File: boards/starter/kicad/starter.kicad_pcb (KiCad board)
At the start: 2 copper layers, 50 x 50 mm, 37 parts, among them J1 USB-C, J2 Qwiic, SW1 RESET, SW2 BOOT, U1 ESP32-S3-WROOM-1-N16R8, U2 LDL1117S33R, U3 H5VUT2U, U4 SHT40-AD1B

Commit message: Phase 1 complete: SWIG crash fixed, all gates pass, fab files, reviews
- Segfault root cause: pcbnew's Remove() and Outline()/GetCourtyard() hand
  KiCad-owned memory to Python; fixed (leak removed items, borrowed()).
  Each stage and each SWIG step now runs in its own process; zones are
  filled by kicad-cli (D-011)
- Routing: pours hidden from Freerouting so GND gets real tracks; Power
  class 0.3 mm; retries; stitching checks track clearance (D-012)
- New gates: netlist round trip, net-class patterns, routing report
- fab.py: gerbers/drill zip, JLCPCB BOM and CPL with rotation corrections
- Datasheet check and blind review by separate agents; cap values, fuse
  before TVS, C1 placement, USB net class fixed (D-014)
- Stack survey confirms the stack (D-013)

Co-Authored-By: Claude Opus 5.5 <noreply@anthropic.com>
Claude-Session: https://claude.ai/code/session_01EfFHJzgmcgpgRkWALfogi6
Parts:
- C2: value 22u -> 1u
- C3: value 10u -> 22u
- moved C1 3.89 mm to (107.5, 131.8), turned to 180 degrees
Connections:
- D3 pad 1: VBUS -> +5V
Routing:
- net GND: track 0.75 -> 233.4 mm, vias 58 -> 74
- net /I2C_SCL: track 57.2 -> 31.1 mm, vias 2 -> 0
- net +5V: track 24.4 -> 36.2 mm
- net VBUS: track 34.1 -> 27.0 mm, vias 0 -> 2
- net /I2C_SDA: track 35.0 -> 41.5 mm, vias 0 -> 4
- net /USB_D+: track 35.4 -> 29.5 mm, vias 2 -> 3
- net /EN: track 42.8 -> 47.2 mm, vias 2 -> 3
- net +3V3: track 111.0 -> 114.0 mm
- net /USB_D-: track 32.3 -> 31.0 mm
- net /BOOT: track 29.5 -> 28.4 mm
- net /UART_TX: track 11.8 -> 12.9 mm, vias 0 -> 2
- net /UART_RX: vias 2 -> 0

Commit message: Starter: LDO cooling copper, 0.3 mm ESP32 EPAD holes, 0.75 A fuse (D-015)
- pcbgen: CopperZone (local pour of one net, above GND) and
  RouteOptions.stitch_local (per-net via stitching); routing report now
  lists every pour and vias per net.
- Starter: +3V3 pour on both layers under U2's tab with 20 vias.
- Local footprint lib/footprints/pcbgen.pretty/ESP32-S3-WROOM-1_EPAD-Drill0.3:
  KiCad's footprint with the 12 EPAD drills at 0.3 mm (JLCPCB's quote form
  charges ~$50 for 0.2 mm).
- F1: Bourns MF-NSMF075-2 (C89653), which has a published derating table;
  a 0.5 A PTC holds only ~0.35-0.40 A at 50-60 C.
- Research: research/2026-09-29-holes-and-fuse.md.
- Full run: ERC 0, DRC 0 open (11 waived silk), 0 unrouted.

Co-Authored-By: Claude Opus 5.5 <noreply@anthropic.com>
Claude-Session: https://claude.ai/code/session_01QxXhFJGsvChPbjPevYQU4a
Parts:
- F1: value 500mA -> 750mA
- U1: footprint RF_Module:ESP32-S3-WROOM-1 -> pcbgen:ESP32-S3-WROOM-1_EPAD-Drill0.3
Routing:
- net /I2C_SDA: track 41.5 -> 59.2 mm, vias 4 -> 2
- net +3V3: track 114.0 -> 105.0 mm, vias 2 -> 22
- net VBUS: track 27.0 -> 18.4 mm, vias 2 -> 3
- net /USB_D+: track 29.5 -> 25.9 mm
- net /EN: track 47.2 -> 43.6 mm, vias 3 -> 2
- net /BOOT: track 28.4 -> 31.6 mm
- net +5V: track 36.2 -> 34.0 mm
- net GND: track 233.4 -> 231.7 mm, vias 74 -> 54
- net /USB_D-: track 31.0 -> 32.1 mm
- net /UART_RX: track 14.1 -> 14.8 mm, vias 0 -> 2
- added copper zone on B.Cu, net +3V3
- added copper zone on F.Cu, net +3V3

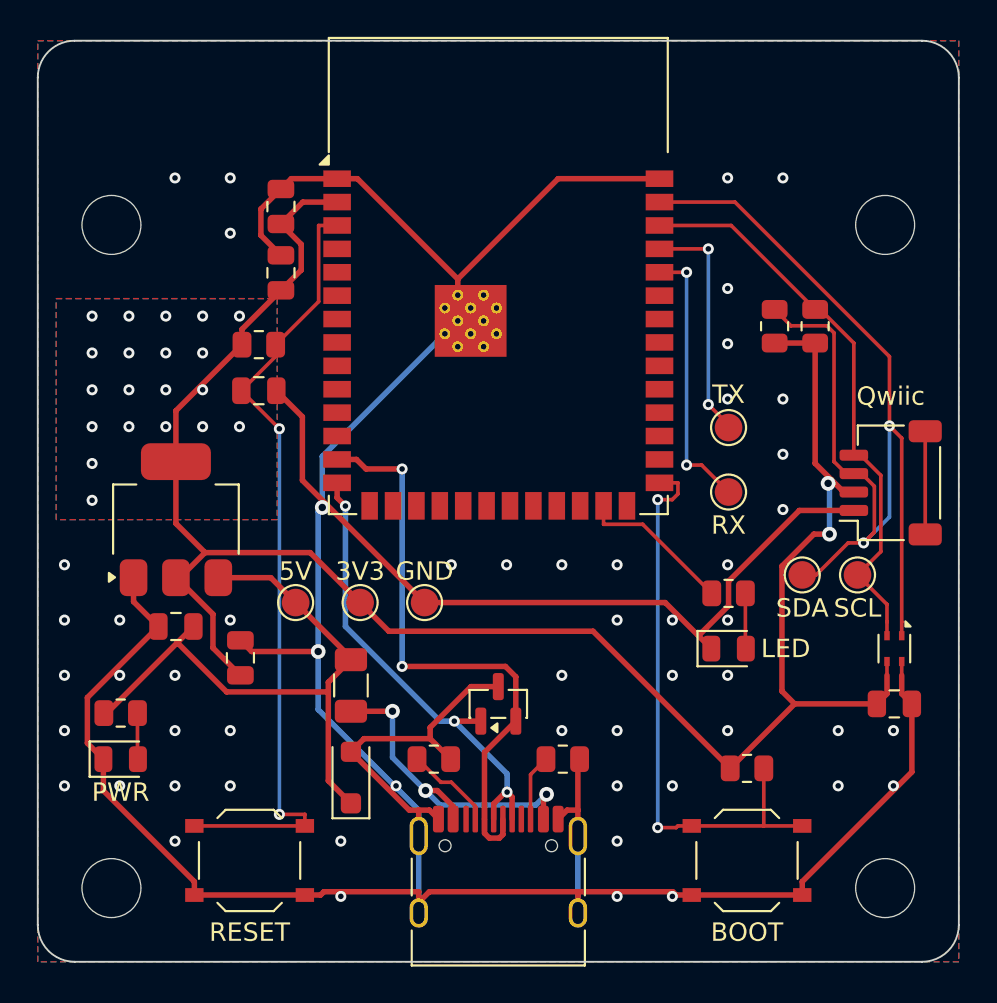
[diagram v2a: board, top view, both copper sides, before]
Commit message: Rust pcbgen: DSN writer, SES reader, stitching, report and fab
The route stage now writes the Specctra DSN itself and reads the SES
back (no SWIG); stitching reads the zone fill kicad-cli saved.

Checked on the starter board:
- DSN equal to KiCad's export in boundary, vias, rules, keep-outs,
  every pin's position/rotation/shape, nets, classes and locked stubs.
- Freerouting turned out deterministic (the same DSN routes the same
  twice); the Python run-to-run variation came from pcbnew's random
  footprint UUIDs reordering the DSN. Retries now shuffle the
  footprint order with a seed, so each try differs but stays
  reproducible.
- Full Rust run in place: netlist + net classes PASS, ERC 0, DRC 0
  open (same 11 waived silk warnings, 0 unconnected, parity 0),
  routing 0 unrouted, no copper in keep-outs, 20 +3V3 cooling vias,
  smallest drill 0.3 mm. BOM and CPL byte-identical to the Python
  ones; tracks differ (a new router run).

Co-Authored-By: Claude Opus 5.5 <noreply@anthropic.com>
Claude-Session: https://claude.ai/code/session_01Gx8G6vBFXfvHWNjYGCm7nX
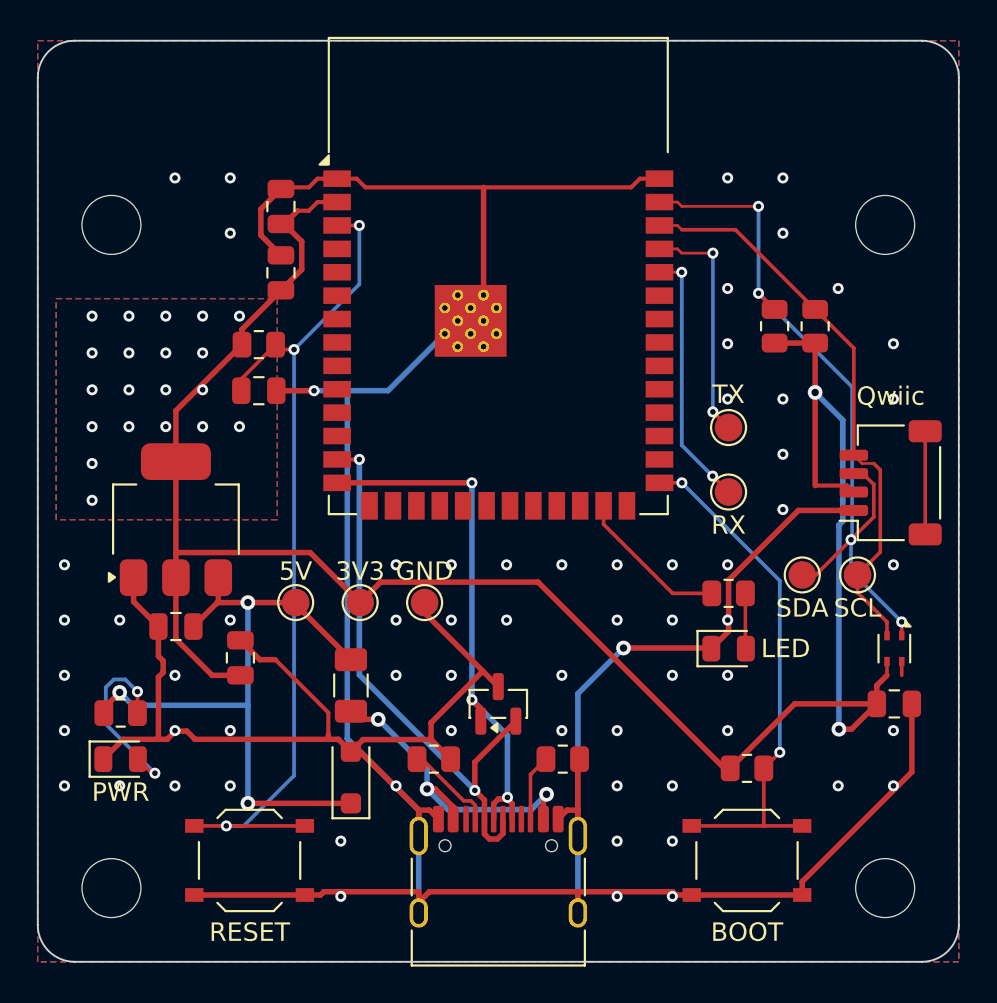
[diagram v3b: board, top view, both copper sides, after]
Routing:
- net /I2C_SDA: track 59.2 -> 41.6 mm, vias 2 -> 4
- net +3V3: track 105.0 -> 115.2 mm
- net /PWR_LED: track 2.51 -> 10.3 mm, vias 0 -> 2
- net /EN: track 43.6 -> 47.7 mm, vias 2 -> 3
- net /USB_D+: track 25.9 -> 29.5 mm
- net /BOOT: track 31.6 -> 28.4 mm
- net +5V: track 34.0 -> 37.0 mm, vias 0 -> 3
- net GND: track 231.7 -> 229.5 mm, vias 54 -> 65
- net /USB_D-: track 32.1 -> 31.1 mm
- net VBUS: track 18.4 -> 17.7 mm
- net /UART_RX: track 14.8 -> 14.2 mm

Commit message: starter: re-route with best-of-8 orders and fanout off (D-017)
Kept order 2 of 8: 0 unrouted, 20 routed vias (was 30), no routed track
under its class width (only the locked 0.2 mm escape stubs, 1.6 mm; was
45.9 mm). All gates pass: netlist and net classes PASS, ERC 0, DRC 0 open
(the same 11 waived silk warnings, 0 unconnected, parity 0), routing 0
unrouted, no copper in keep-outs. Parts, nets, placement and rules are
unchanged; schematic, BOM, CPL and positions byte-identical. Only the
copper layers and drill file changed (the other gerbers only in their
timestamps).

Co-Authored-By: Claude Opus 5.5 <noreply@anthropic.com>
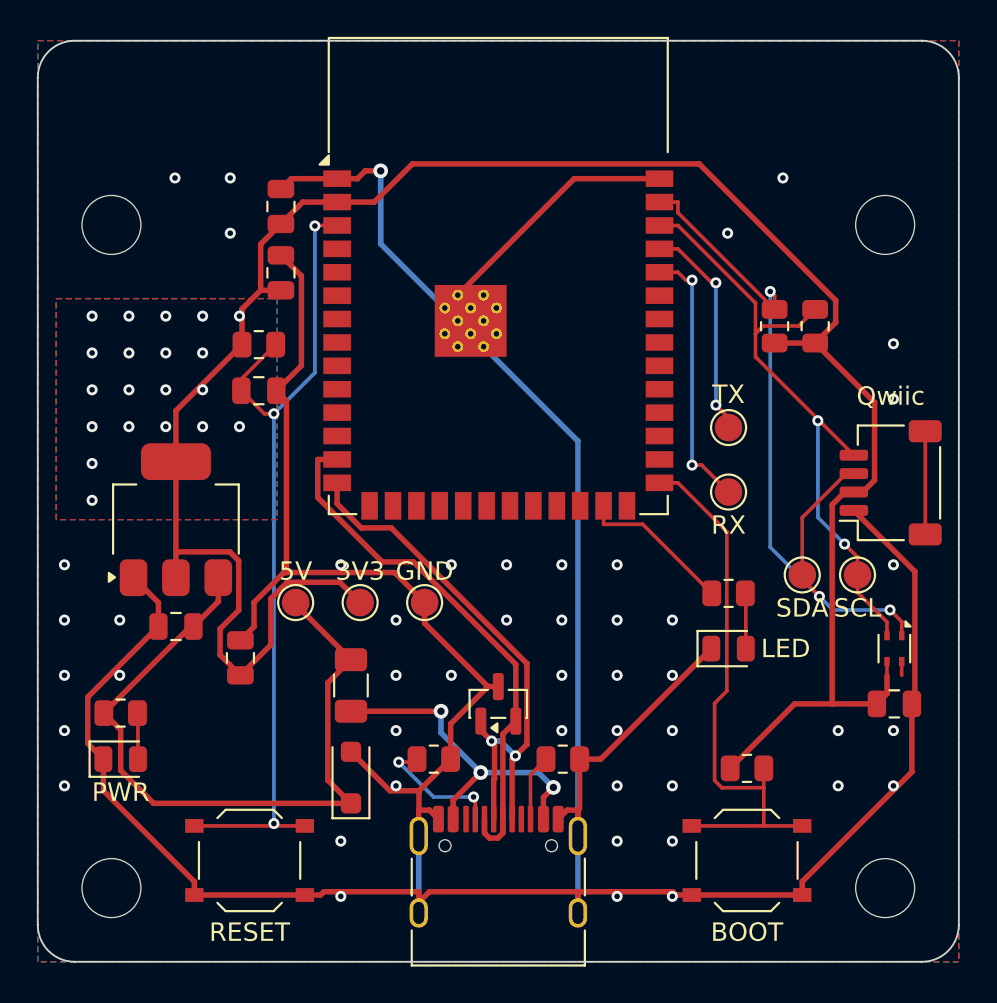
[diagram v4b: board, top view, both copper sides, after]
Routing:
- net /PWR_LED: track 10.3 -> 2.51 mm, vias 2 -> 0
- net /I2C_SCL: track 31.1 -> 34.5 mm, vias 0 -> 2
- net +5V: track 37.0 -> 39.9 mm, vias 3 -> 0
- net +3V3: track 115.2 -> 117.8 mm, vias 22 -> 20
- net /CC1: track 4.95 -> 7.14 mm, vias 0 -> 2
- net /BOOT: track 28.4 -> 30.5 mm, vias 2 -> 0
- net /USB_D-: track 31.1 -> 29.1 mm, vias 2 -> 0
- net /USB_D+: track 29.5 -> 31.1 mm, vias 3 -> 2
- net /EN: track 47.7 -> 46.3 mm
- net /UART_TX: track 12.8 -> 12.0 mm
- net VBUS: track 17.7 -> 18.5 mm
- net /I2C_SDA: track 41.6 -> 42.0 mm, vias 4 -> 3
- net GND: vias 65 -> 48
